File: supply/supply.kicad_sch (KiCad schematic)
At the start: 4 parts, among them M1 Fan, U1 XL1509-5.0, U2 TPS61099DRV

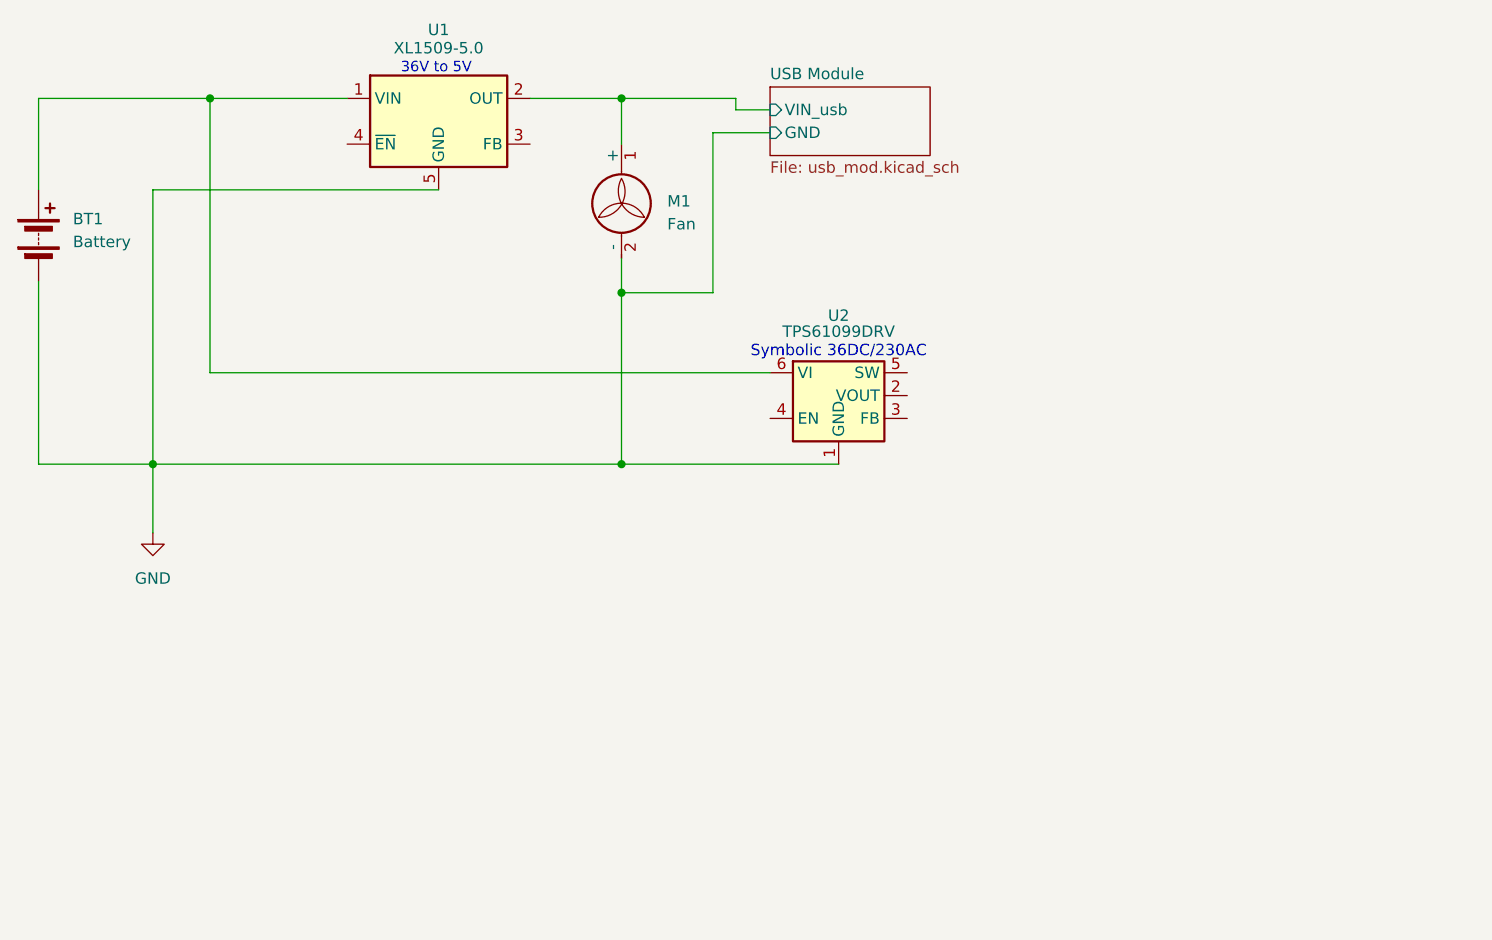
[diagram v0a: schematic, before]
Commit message: added 230V connector and switch
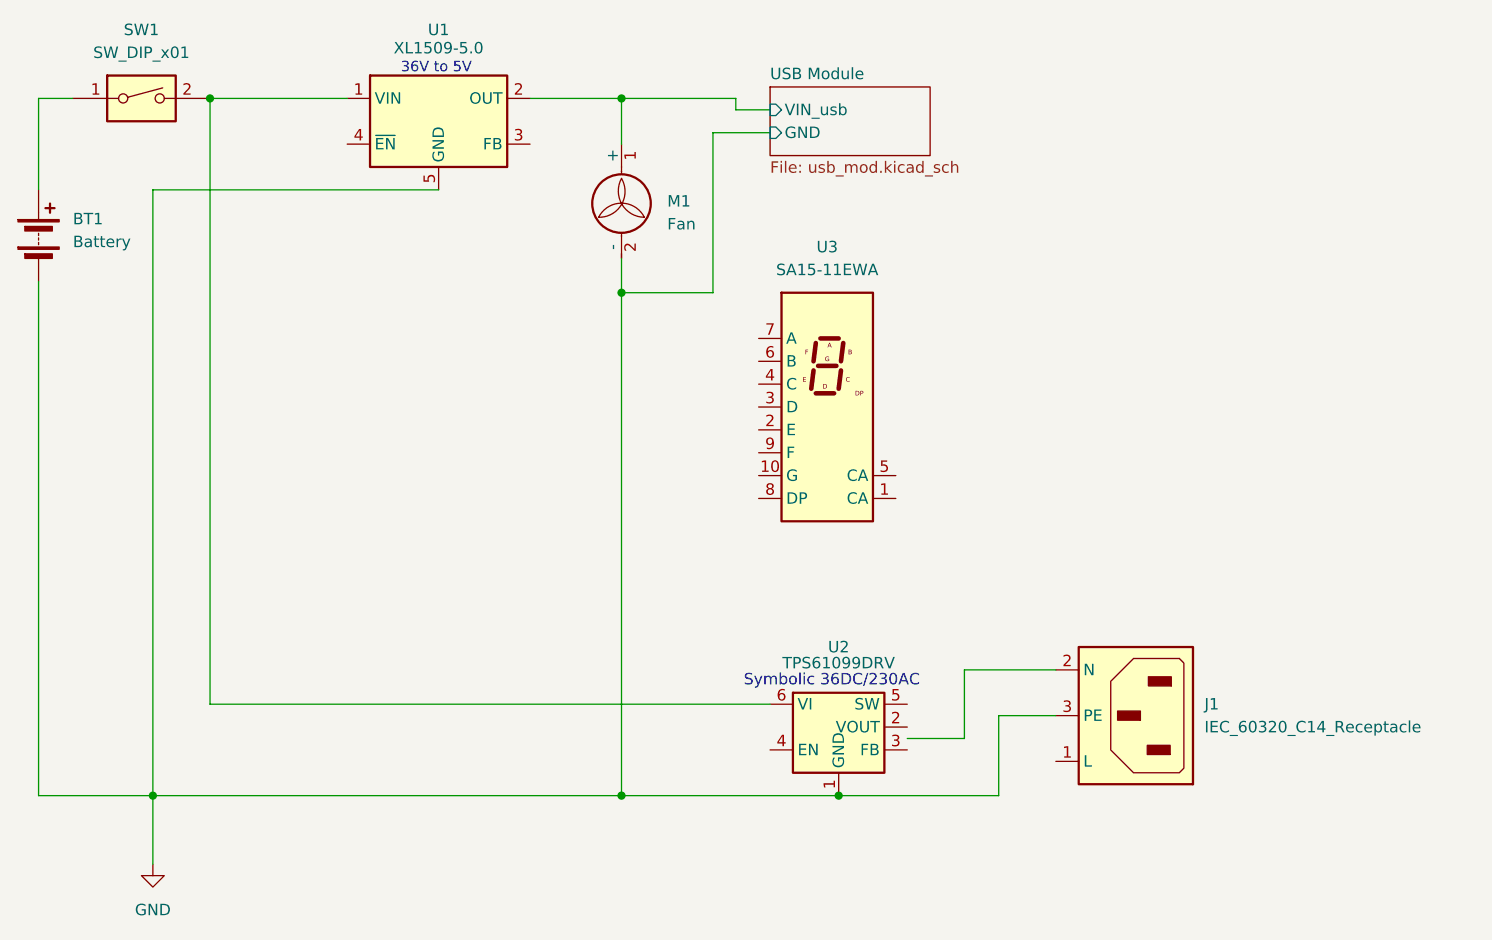
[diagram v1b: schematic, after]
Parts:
- added J1: IEC_60320_C14_Receptacle, symbol Connector:IEC_60320_C14_Receptacle
- added SW1: SW_DIP_x01, symbol Switch:SW_DIP_x01
- added U3: SA15-11EWA, Display_7Segment:SA15-11xxx, symbol Display_Character:SA15-11EWA
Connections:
- net GND: now also J1.3 (PE)
- net at U1.1 (VIN), U2.6 (VI): now also SW1.2; no longer BT1.1 (+)
- new net: BT1.1 (+), SW1.1
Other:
- moved on the sheet: U2
